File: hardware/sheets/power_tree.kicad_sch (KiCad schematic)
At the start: 0 parts

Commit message: hw: draw Rev A power tree and USB charger sheets
Power tree: TPS63802 3.3 V logic rail, TPS61023 LED rail with load
disconnect, switched VBAT measurement, VLED sense, 0-ohm measurement
links and test points. The logic rail is enabled by the power switch
or by the charger's power-good output, so USB starts a charging-only
state with the switch off and removing USB turns the rail off again.
The LED rail and VBAT measurement default off.

Charger: USB-C sink with separate 5.1 kOhm Rd, TPD4E05U06 on D+, D-,
CC1 and CC2, isolated CC sensing, BQ25620 switching charger with BC1.2
detection, a board NTC on TS, and the JST-PH battery header.

The VLED setting is provisional until LED testing. The battery header
polarity is provisional until checked against the pack, and the USB-C
receptacle part is still to be chosen.
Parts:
- added C201, C203: 10uF 25V, Capacitor_SMD:C_0805_2012Metric, symbol Device:C
- added C202, C204, C205: 22uF 25V, Capacitor_SMD:C_0805_2012Metric, symbol Device:C
- added C206: 4.7nF, Capacitor_SMD:C_0402_1005Metric, symbol Device:C
- added C207, C208: 100nF, Capacitor_SMD:C_0402_1005Metric, symbol Device:C
- added L201: 0.47uH, smart-led-badge:L_Murata_DFE201612E, symbol Device:L
- added L202: 1uH, smart-led-badge:L_Coilcraft_XEL4030, symbol Device:L
- added Q201, Q203: AO3401A, Package_TO_SOT_SMD:SOT-23, symbol Transistor_FET:AO3401A
- added Q202, Q204: AO3400A, Package_TO_SOT_SMD:SOT-23, symbol Transistor_FET:AO3400A
- added R201: 10k, Resistor_SMD:R_0402_1005Metric, symbol Device:R
- added R202, R205: 20k, Resistor_SMD:R_0402_1005Metric, symbol Device:R
- added R203, R208, R214, R219, R222, R223: 100k, Resistor_SMD:R_0402_1005Metric, symbol Device:R
- added R204: 12k, Resistor_SMD:R_0402_1005Metric, symbol Device:R
- added R206, R207: 0, Resistor_SMD:R_0402_1005Metric, symbol Device:R
- added R209, R215: 0, Resistor_SMD:R_0805_2012Metric, symbol Device:R
- added R210: 33k, Resistor_SMD:R_0402_1005Metric, symbol Device:R
- added R211, R217: 4.7k, Resistor_SMD:R_0402_1005Metric, symbol Device:R
- added R212, R213: DNP, Resistor_SMD:R_0402_1005Metric, symbol Device:R
- added R216: 200k, Resistor_SMD:R_0402_1005Metric, symbol Device:R
- added R218, R220, R221: 47k, Resistor_SMD:R_0402_1005Metric, symbol Device:R
- added SW201: Power switch (SPDT, part TBD), symbol Switch:SW_SPDT
- added TP201: SYS, TestPoint:TestPoint_Pad_D1.0mm, symbol Connector:TestPoint
- added TP202: VBAT, TestPoint:TestPoint_Pad_D1.0mm, symbol Connector:TestPoint
- added TP203: 3V3_REG, TestPoint:TestPoint_Pad_D1.0mm, symbol Connector:TestPoint
- added TP204: +3V3, TestPoint:TestPoint_Pad_D1.0mm, symbol Connector:TestPoint
- added TP205: VLED_REG, TestPoint:TestPoint_Pad_D1.0mm, symbol Connector:TestPoint
- added TP206: VLED, TestPoint:TestPoint_Pad_D1.0mm, symbol Connector:TestPoint
- added TP207, TP208: GND, TestPoint:TestPoint_Pad_D1.0mm, symbol Connector:TestPoint
- added TP209: EN_3V3, TestPoint:TestPoint_Pad_D1.0mm, symbol Connector:TestPoint
- added TP210: PG_3V3, TestPoint:TestPoint_Pad_D1.0mm, symbol Connector:TestPoint
- added TP211: LED_EN, TestPoint:TestPoint_Pad_D1.0mm, symbol Connector:TestPoint
- added TP212: VBAT_SENSE, TestPoint:TestPoint_Pad_D1.0mm, symbol Connector:TestPoint
- added TP213: VLED_SENSE, TestPoint:TestPoint_Pad_D1.0mm, symbol Connector:TestPoint
- added TP214: VBAT_MEAS_EN, TestPoint:TestPoint_Pad_D1.0mm, symbol Connector:TestPoint
- added TP215: SW_ON, TestPoint:TestPoint_Pad_D1.0mm, symbol Connector:TestPoint
- added TP216: PWR_SW_N, TestPoint:TestPoint_Pad_D1.0mm, symbol Connector:TestPoint
- added U201: TPS63802, smart-led-badge:Texas_DLA0010A, symbol smart-led-badge:TPS63802
- added U202: TPS61023, smart-led-badge:Texas_DRL0006A, symbol smart-led-badge:TPS61023
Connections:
- new net +3V3: R209.2, TP204.1
- new net 3V3_REG: C202.1, R203.1, R207.1, R208.1, R209.1, TP203.1, U201.6 (VOUT)
- new net CHG_PG_N: Q203.1 (G), R223.2
- new net EN_3V3: Q203.3 (D), R201.2, R202.1, TP209.1, U201.1 (EN)
- new net FB_3V3: R204.2, R205.1, U201.4 (FB)
- new net FB_3V3_A: R203.2, R204.1
- new net FB_VLED: C206.2, R210.2, R211.1, R212.2, R213.1, U202.1 (FB)
- new net GND: C201.2, C202.2, C203.2, C204.2, C205.2, C207.2, C208.2, Q202.2 (S), Q204.2 (S), R202.2, R205.2, R206.2, R211.2, R213.2, R214.2, R217.2, R219.2, R221.2, R222.2, TP207.1, TP208.1, U201.3 (AGND), U201.8 (GND), U202.4 (GND)
- new net L1_3V3: L201.1, U201.9 (L1)
- new net L2_3V3: L201.2, U201.7 (L2)
- new net LED_EN: R214.1, TP211.1, U202.2 (EN)
- new net MODE_3V3: R206.1, R207.2, U201.2 (MODE)
- new net PG_3V3: R208.2, TP210.1, U201.5 (PG)
- new net PWR_SW_N: Q204.3 (D), TP216.1
- new net SW_ON: Q204.1 (G), R201.1, R222.1, SW201.1 (A), TP215.1
- new net SW_VLED: L202.2, U202.5 (SW)
- new net SYS: C201.1, C203.1, L202.1, Q203.2 (S), R223.1, SW201.2 (B), TP201.1, U201.10 (VIN), U202.3 (VIN)
- new net VBAT: Q201.2 (S), R218.1, TP202.1
- new net VBAT_MEAS_EN: Q202.1 (G), R219.1, TP214.1
- new net VBAT_SENSE: C208.1, R220.2, R221.1, TP212.1
- new net VBAT_SW: Q201.3 (D), R220.1
- new net VBAT_SW_G: Q201.1 (G), Q202.3 (D), R218.2
- new net VLED: R215.2, R216.1, TP206.1
- new net VLED_REG: C204.1, C205.1, C206.1, R210.1, R212.1, R215.1, TP205.1, U202.6 (VOUT)
- new net VLED_SENSE: C207.1, R216.2, R217.1, TP213.1
- no-connect marks 0 -> 1
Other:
- note added: "PWR_FLAG on VBAT: the battery connector drives it. PWR_FLAG on +3V3 and VLED: the rails are driven through 0-ohm measurement links. SYS is driven by the BQ25620 SYS pin (USB/charger/battery sheet)."
- note added: "Regulators and power tree (Rev A) - design notes Power states: EN_3V3 = switch ON (SYS via R201) OR charger PG (Q203). OFF + battery only: EN low, 3V3 off. OFF + valid USB: PG low -> 3V3 on for the charging-only firmware mode (display off). USB removed with the switch OFF: PG releases, R202 pulls EN low, 3V3 shuts down in hardware. EN <= SYS (< 4.6 V) < 6 V abs max. PWR_SW_N (Q204, open drain) re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"

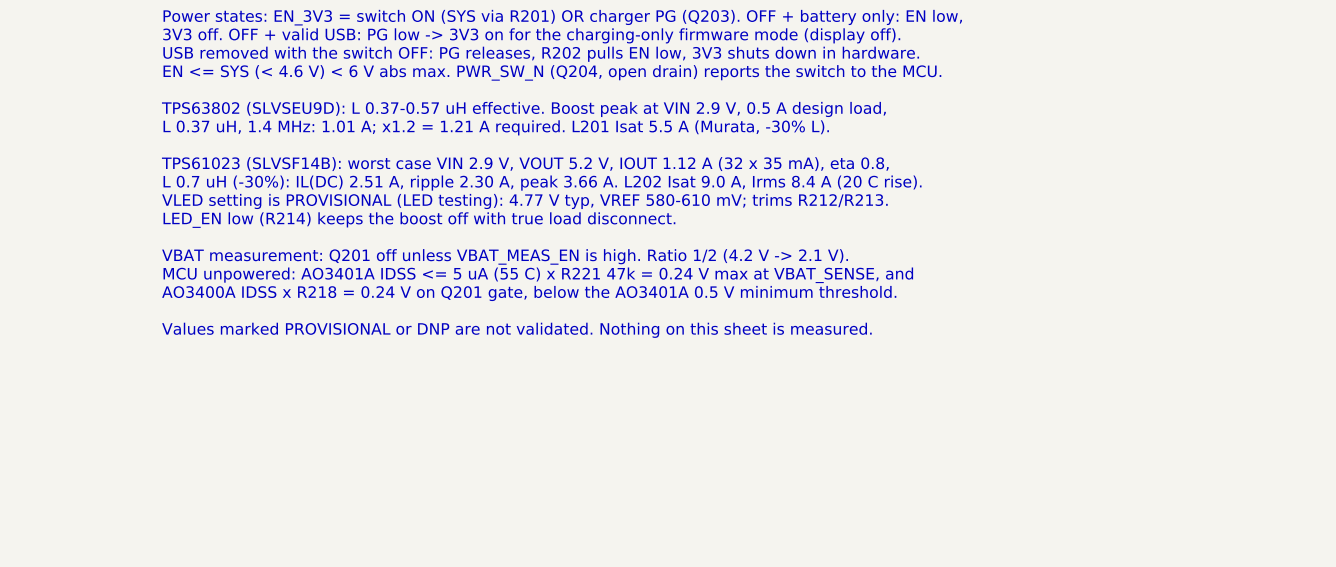
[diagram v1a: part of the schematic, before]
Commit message: hw: note the LED boost pass-through limit
The TPS61023 only boosts: when SYS is above the setting it passes SYS
through, and SYS reaches about 4.25 V on a full pack. Record on the
sheet that the trim positions are useful for settings of about
4.4-5.2 V, not lower.
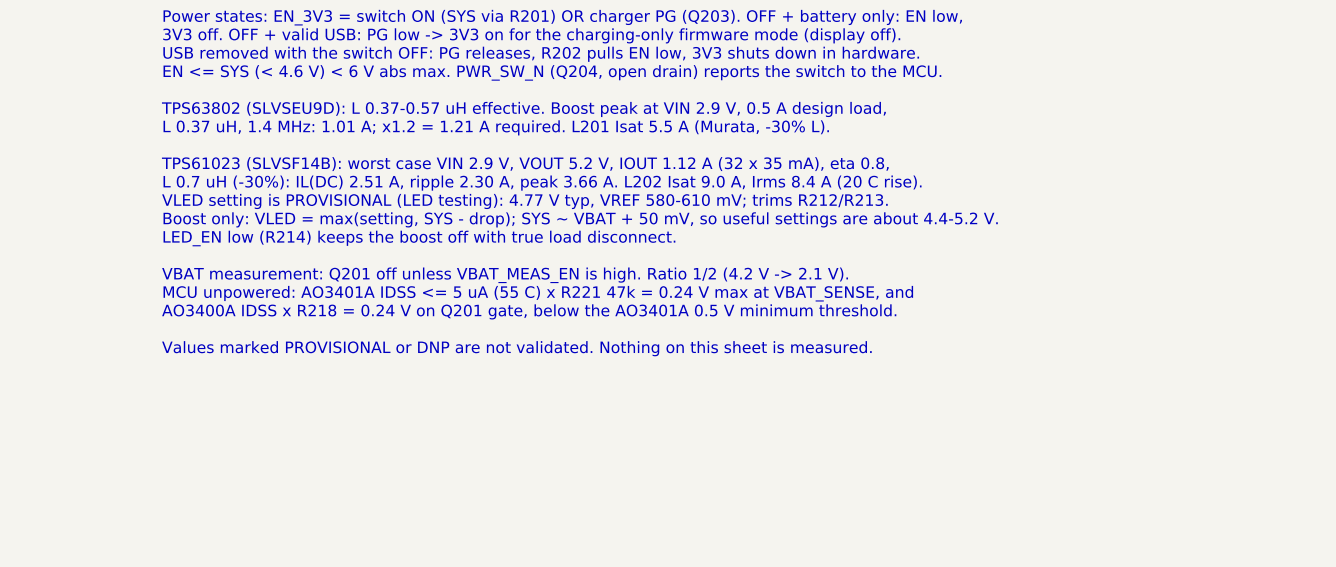
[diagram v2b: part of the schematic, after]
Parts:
- R212: Note Trim: parallel to R210 lowers VLED -> Trim: parallel to R210 lowers VLED, only to about 4.4 V (be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
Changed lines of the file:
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@@
 			)
 		)
-		(property "Note" "Trim: parallel to R210 lowers VLED"
+		(property "Note" "Trim: parallel to R210 lowers VLED, only to about 4.4 V (below SYS max the boost passes SYS through)"
 			(at 193.04 124.46 0)
 			(hide yes)
@@
 		)
 	)
-	(text "Regulators and power tree (Rev A) - design notes\n\nPower states: EN_3V3 = switch ON (SYS via R201) OR charger PG (Q203). OFF + battery only: EN low,\n3V3 off. OFF + valid USB: PG low -> 3V3 on for the charging-only firmware mode (display off).\nUSB removed with the switch OFF: PG releases, R202 pulls EN low, 3V3 shuts down in hardware.\nEN <= SYS (< 4.6 V) < 6 V abs max. PWR_SW_N (Q204, open drain) reports the switch to the MCU.\n\nTPS63802 (SLVSEU9D): L 0.37-0.57 uH effective. Boost peak at VIN 2.9 V, 0.5 A design load,\nL 0.37 uH, 1.4 MHz: 1.01 A; x1.2 = 1.21 A required. L201 Isat 5.5 A (Murata, -30% L).\n\nTPS61023 (SLVSF14B): worst case VIN 2.9 V, VOUT 5.2 V, IOUT 1.12 A (32 x 35 mA), eta 0.8,\nL 0.7 uH (-30%): IL(DC) 2.51 A, ripple 2.30 A, peak 3.66 A. L202 Isat 9.0 A, Irms 8.4 A (20 C rise).\nVLED setting is PROVISIONAL (LED testing): 4.77 V typ, VREF 580-610 mV; trims R212/R213.\nLED_EN low (R214) keeps the boost off with true load disconnect.\n\nVBAT measurement: Q201 off unless VBAT_MEAS_EN is high. Ratio 1/2 (4.2 V -> 2.1 V).\nMCU unpowered: AO3401A IDSS <= 5 uA (55 C) x R221 47k = 0.24 V max at VBAT_SENSE, and\nAO3400A IDSS x R218 = 0.24 V on Q201 gate, below the AO3401A 0.5 V minimum threshold.\n\nValues marked PROVISIONAL or DNP are not validated. Nothing on this sheet is measured."
+	(text "Regulators and power tree (Rev A) - design notes\n\nPower states: EN_3V3 = switch ON (SYS via R201) OR charger PG (Q203). OFF + battery only: EN low,\n3V3 off. OFF + valid USB: PG low -> 3V3 on for the charging-only firmware mode (display off).\nUSB removed with the switch OFF: PG releases, R202 pulls EN low, 3V3 shuts down in hardware.\nEN <= SYS (< 4.6 V) < 6 V abs max. PWR_SW_N (Q204, open drain) reports the switch to the MCU.\n\nTPS63802 (SLVSEU9D): L 0.37-0.57 uH effective. Boost peak at VIN 2.9 V, 0.5 A design load,\nL 0.37 uH, 1.4 MHz: 1.01 A; x1.2 = 1.21 A required. L201 Isat 5.5 A (Murata, -30% L).\n\nTPS61023 (SLVSF14B): worst case VIN 2.9 V, VOUT 5.2 V, IOUT 1.12 A (32 x 35 mA), eta 0.8,\nL 0.7 uH (-30%): IL(DC) 2.51 A, ripple 2.30 A, peak 3.66 A. L202 Isat 9.0 A, Irms 8.4 A (20 C rise).\nVLED setting is PROVISIONAL (LED testing): 4.77 V typ, VREF 580-610 mV; trims R212/R213.\nBoost only: VLED = max(setting, SYS - drop); SYS ~ VBAT + 50 mV, so useful settings are about 4.4-5.2 V.\nLED_EN low (R214) keeps the boost off with true load disconnect.\n\nVBAT measurement: Q201 off unless VBAT_MEAS_EN is high. Ratio 1/2 (4.2 V -> 2.1 V).\nMCU unpowered: AO3401A IDSS <= 5 uA (55 C) x R221 47k = 0.24 V max at VBAT_SENSE, and\nAO3400A IDSS x R218 = 0.24 V on Q201 gate, below the AO3401A 0.5 V minimum threshold.\n\nValues marked PROVISIONAL or DNP are not validated. Nothing on this sheet is measured."
 		(exclude_from_sim no)
 		(at 299.72 152.4 0)
